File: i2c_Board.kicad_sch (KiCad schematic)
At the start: 18 parts, among them J1 Conn_01x10_Pin, J2 Logic Analyzer Connector Pins, U1 MCP9808_MSOP, U2 MCP7940N-xMS, Y1 Crystal

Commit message: Updated footprints
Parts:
- removed J1: Conn_01x10_Pin, Connector_PinHeader_1.00mm:PinHeader_1x10_P1.00mm_Vertical, symbol Connector:Conn_01x10_Pin
- added H1, H2, H3, H4: MountingHole_Pad, MountingHole:MountingHole_2.2mm_M2_DIN965_Pad, symbol Mechanical:MountingHole_Pad
- added J1: Conn_01x09_Pin, Connector_PinHeader_2.54mm:PinHeader_1x09_P2.54mm_Vertical, symbol Connector:Conn_01x09_Pin
- BT1: footprint Battery:BatteryHolder_Keystone_3002_1x2032 -> BAT-HLD-002-SMT:BAT_BAT-HLD-002-SMT; symbol Device:Battery_Cell -> BAT-HLD-002-SMT:BAT-HLD-002-SMT; Availability (none) -> In Stock; Check_prices (none) -> https://www.snapeda.com/parts/BAT-HLD-002-SMT/TE+Connectivi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; Description_1 (none) -> Battery Holder Coin 20 SMT Nickel; MF (none) -> TE Connectivity; MP (none) -> BAT-HLD-002-SMT; Package (none) -> None; Price (none) -> None; Purchase-URL (none) -> https://www.snapeda.com/api/url_track_click_mouser/?unipart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; SnapEDA_Link (none) -> https://www.snapeda.com/parts/BAT-HLD-002-SMT/TE+Connectivi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
- J2: footprint Connector_PinHeader_1.00mm:PinHeader_1x02_P1.00mm_Vertical -> Connector_PinHeader_2.54mm:PinHeader_1x02_P2.54mm_Vertical
- U1: value MCP9808_MSOP -> MCP9808
- U2: value MCP7940N-xMS -> MCP7940N
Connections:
- net +5V: now also J1.1 (Pin_1)
- net Address_0: now also J1.2 (Pin_2)
- net Address_1: now also J1.3 (Pin_3)
- net Address_2: now also J1.4 (Pin_4)
- net GND: now also BT1.P1, BT1.P2, H1.1, H2.1, H3.1, H4.1, J1.8 (Pin_8), J1.9 (Pin_9); no longer BT1.2 (-)
- net MCU_SCL: now also J1.6 (Pin_6)
- net MCU_SDA: now also J1.7 (Pin_7)
- net MFP: now also J1.5 (Pin_5)
- net at U2.3 (VBAT): now also BT1.N; no longer BT1.1 (+)

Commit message: Modified footprint & Rearranged routing
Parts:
- R5, R7: footprint Diode_SMD:D_0805_2012Metric_Pad1.15x1.40mm_HandSolder -> Resistor_SMD:R_0805_2012Metric_Pad1.20x1.40mm_HandSolder
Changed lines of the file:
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@@
 	(title_block
 		(title "I2C Testing Board")
-		(comment 1 "Add Connector Pin")
-		(comment 2 "Add Custom Name to PCB")
 	)
 	(junction
@@
 			)
 		)
-		(property "Footprint" "Diode_SMD:D_0805_2012Metric_Pad1.15x1.40mm_HandSolder"
+		(property "Footprint" "Resistor_SMD:R_0805_2012Metric_Pad1.20x1.40mm_HandSolder"
 			(at 97.79 50.038 90)
 			(effects
@@
 			)
 		)
-		(property "Footprint" "Diode_SMD:D_0805_2012Metric_Pad1.15x1.40mm_HandSolder"
+		(property "Footprint" "Resistor_SMD:R_0805_2012Metric_Pad1.20x1.40mm_HandSolder"
 			(at 63.5 80.518 90)
 			(effects

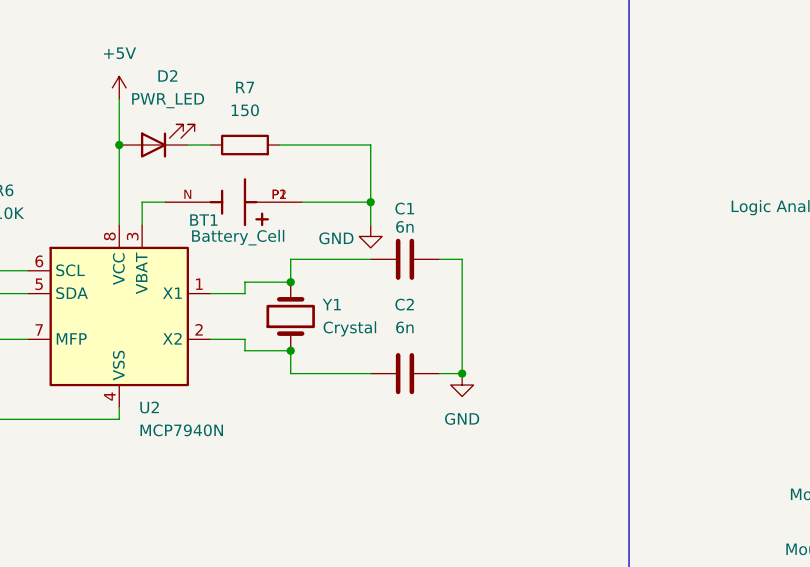
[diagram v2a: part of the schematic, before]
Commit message: Changed Capacitor value from 6nF to 6pF
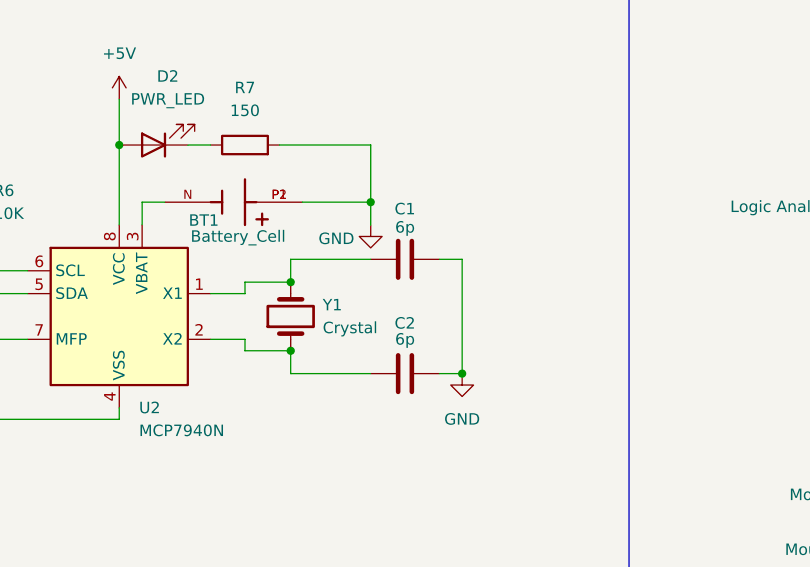
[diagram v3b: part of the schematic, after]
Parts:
- C1, C2: value 6n -> 6p
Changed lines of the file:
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@@
 		(on_board yes)
 		(dnp no)
-		(fields_autoplaced yes)
 		(property "Reference" "C2"
-			(at 115.57 66.04 90)
-			(effects
-				(font
-					(size 1.27 1.27)
-				)
-			)
-		)
-		(property "Value" "6n"
-			(at 115.57 68.58 90)
+			(at 115.57 68.072 90)
+			(effects
+				(font
+					(size 1.27 1.27)
+				)
+			)
+		)
+		(property "Value" "6p"
+			(at 115.57 69.85 90)
 			(effects
 				(font
@@
 			)
 		)
-		(property "Value" "6n"
+		(property "Value" "6p"
 			(at 115.57 57.404 90)
 			(effects

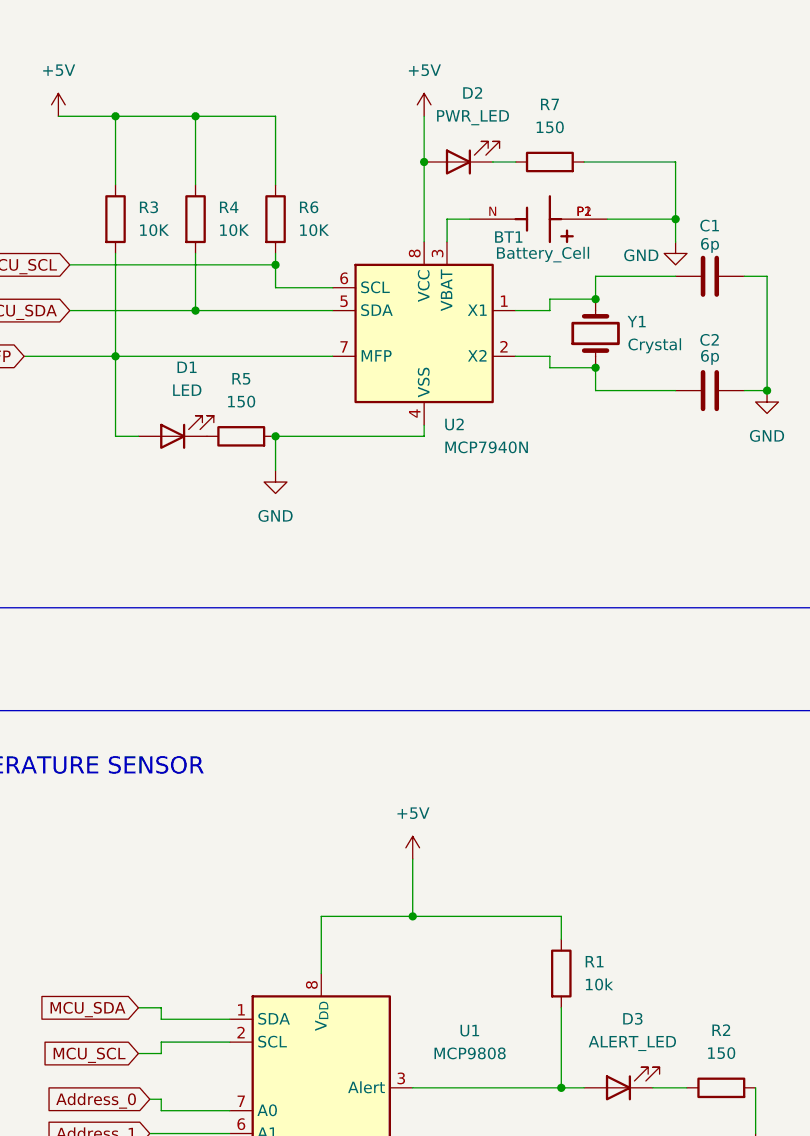
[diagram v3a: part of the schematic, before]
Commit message: Added Decoupling Capacitors
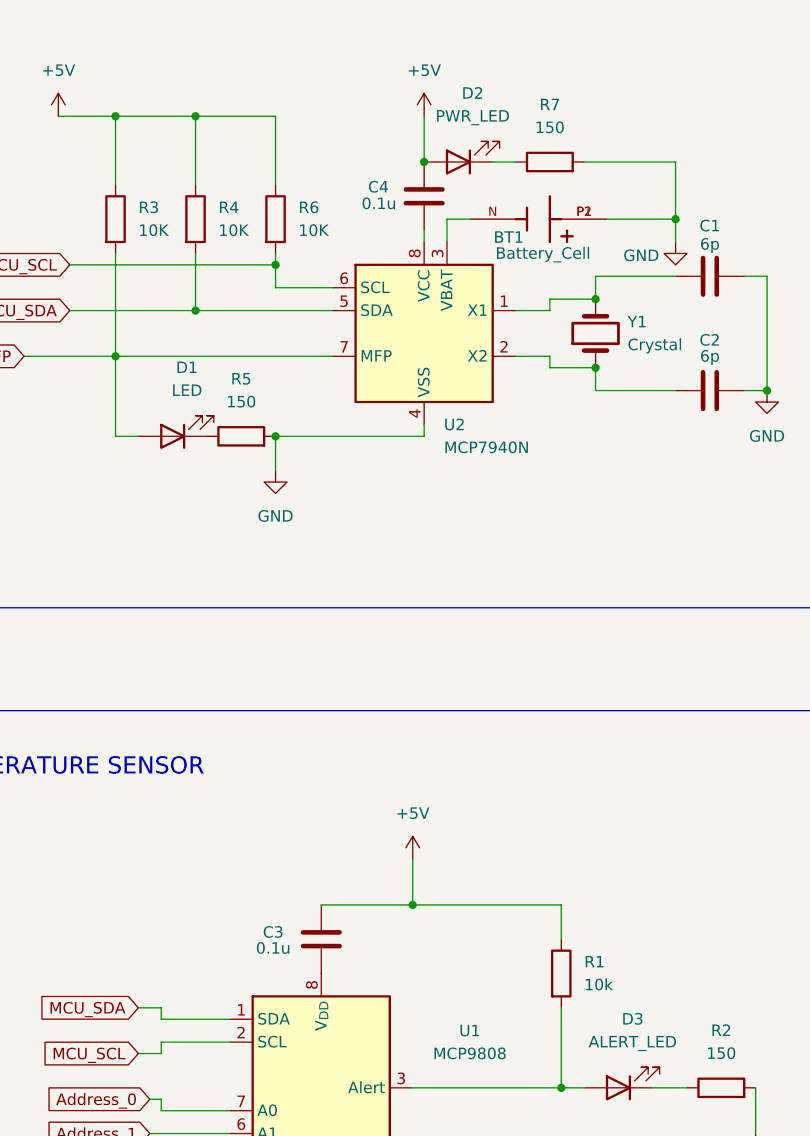
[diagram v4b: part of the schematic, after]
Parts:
- added C3, C4: 0.1u, Capacitor_SMD:C_0805_2012Metric_Pad1.18x1.45mm_HandSolder, symbol Device:C
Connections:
- net +5V: now also C3.1, C4.1; no longer U1.8 (V_{DD}), U2.8 (VCC)
- new net: C4.2, U2.8 (VCC)
- new net: C3.2, U1.8 (V_{DD})
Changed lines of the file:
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@@
 	)
 	(junction
-		(at 82.55 132.08)
-		(diameter 0)
-		(color 0 0 0 0)
-	)
-	(junction
 		(at 186.69 86.36)
 		(diameter 0)
@@
 	)
 	(junction
+		(at 82.55 130.81)
+		(diameter 0)
+		(color 0 0 0 0)
+	)
+	(junction
 		(at 83.82 48.26)
 		(diameter 0)
@@
 	(wire
 		(pts
-			(xy 72.39 138.43) (xy 72.39 132.08)
-		)
-		(stroke
-			(width 0)
-			(type default)
-		)
-	)
-	(wire
-		(pts
 			(xy 187.96 64.77) (xy 175.26 64.77)
 		)
@@
 	(wire
 		(pts
-			(xy 99.06 132.08) (xy 99.06 134.62)
+			(xy 99.06 130.81) (xy 99.06 134.62)
 		)
 		(stroke
@@
 	(wire
 		(pts
+			(xy 83.82 55.88) (xy 83.82 57.15)
+		)
+		(stroke
+			(width 0)
+			(type default)
+		)
+	)
+	(wire
+		(pts
 			(xy 175.26 60.96) (xy 187.96 60.96)
 		)
@@
 	(wire
 		(pts
-			(xy 72.39 132.08) (xy 82.55 132.08)
+			(xy 72.39 130.81) (xy 82.55 130.81)
 		)
 		(stroke
@@
 	(wire
 		(pts
-			(xy 82.55 132.08) (xy 99.06 132.08)
+			(xy 82.55 130.81) (xy 99.06 130.81)
 		)
 		(stroke
@@
 	(wire
 		(pts
-			(xy 82.55 125.73) (xy 82.55 132.08)
-		)
-		(stroke
-			(width 0)
-			(type default)
-		)
-	)
-	(wire
-		(pts
-			(xy 83.82 48.26) (xy 83.82 57.15)
+			(xy 82.55 125.73) (xy 82.55 130.81)
 		)
 		(stroke
@@
 	)
 	(symbol
+		(lib_id "Device:C")
+		(at 72.39 134.62 0)
+		(unit 1)
+		(exclude_from_sim no)
+		(in_bom yes)
+		(on_board yes)
+		(dnp no)
+		(property "Reference" "C3"
+			(at 67.056 133.858 0)
+			(effects
+				(font
+					(size 1.27 1.27)
+				)
+			)
+		)
+		(property "Value" "0.1u"
+			(at 67.056 135.636 0)
+			(effects
+				(font
+					(size 1.27 1.27)
+				)
+			)
+		)
+		(property "Footprint" "Capacitor_SMD:C_0805_2012Metric_Pad1.18x1.45mm_HandSolder"
+			(at 73.3552 138.43 0)
+			(effects
+				(font
+					(size 1.27 1.27)
+				)
+				(hide yes)
+			)
+		)
+		(property "Datasheet" "~"
+			(at 72.39 134.62 0)
+			(effects
+				(font
+					(size 1.27 1.27)
+				)
+				(hide yes)
+			)
+		)
+		(property "Description" "Unpolarized capacitor"
+			(at 72.39 134.62 0)
+			(effects
+				(font
+					(size 1.27 1.27)
+				)
+				(hide yes)
+			)
+		)
+		(pin "1"
+		)
+		(pin "2"
+		)
+		(instances
+			(project "i2c_Board"
+				(path "/853e014d-ba1a-4791-8d4a-2caab7ca8c76"
+					(reference "C3")
+					(unit 1)
+				)
+			)
+		)
+	)
+	(symbol
 		(lib_id "Device:LED")
 		(at 87.63 48.26 180)
@@
 					(unit 1)
 				)
+			)
+		)
+	)
+	(symbol
+		(lib_id "Device:C")
+		(at 83.82 52.07 0)
+		(unit 1)
+		(exclude_from_sim no)
+		(in_bom yes)
+		(on_board yes)
+		(dnp no)
+		(property "Reference" "C4"
+			(at 78.74 51.054 0)
+			(effects
+				(font
+					(size 1.27 1.27)
+				)
+			)
+		)
+		(property "Value" "0.1u"
+			(at 78.8035 52.8955 0)
+			(effects
+				(font
+					(size 1.27 1.27)
+				)
+			)
+		)
+		(property "Footprint" "Capacitor_SMD:C_0805_2012Metric_Pad1.18x1.45mm_HandSolder"
+			(at 84.7852 55.88 0)
+			(effects
+				(font
+					(size 1.27 1.27)
+				)
+				(hide yes)
+			)
+		)
+		(property "Datasheet" "~"
+			(at 83.82 52.07 0)
+			(effects
+				(font
+					(size 1.27 1.27)
+				)
+				(hide yes)
+			)
+		)
+		(property "Description" "Unpolarized capacitor"
+			(at 83.82 52.07 0)
+			(effects
+				(font
+					(size 1.27 1.27)
+				)
+				(hide yes)
+			)
+		)
+		(pin "1"
+		)
+		(pin "2"
+		)
+		(instances
+			(project "i2c_Board"
+				(path "/853e014d-ba1a-4791-8d4a-2caab7ca8c76"
+					(reference "C4")
+					(unit 1)
+				)

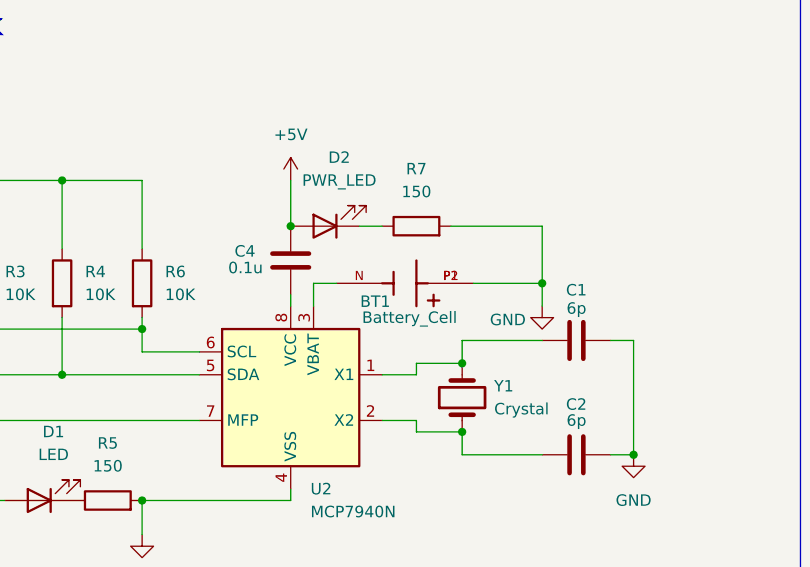
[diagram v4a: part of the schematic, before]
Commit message: Flipped incorrect battery polarity
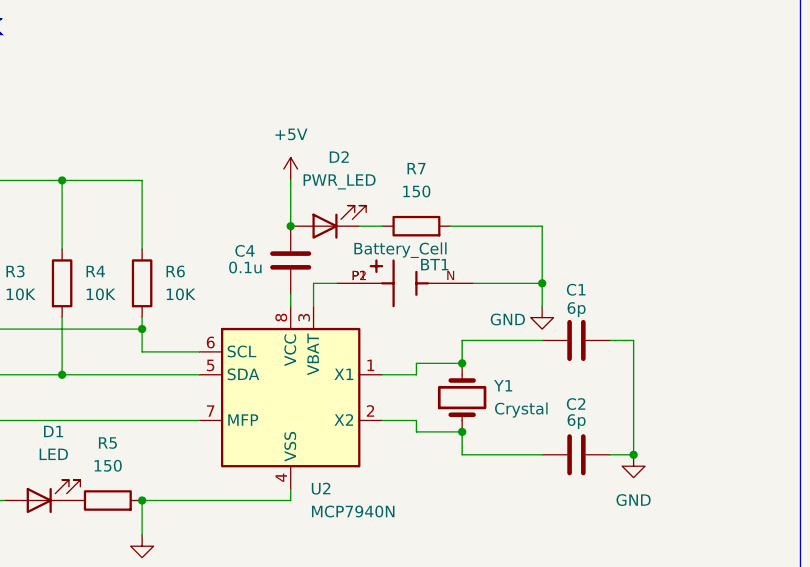
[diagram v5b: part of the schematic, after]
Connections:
- net GND: now also BT1.N; no longer BT1.P1, BT1.P2
- net at U2.3 (VBAT): now also BT1.P1, BT1.P2; no longer BT1.N
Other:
- moved on the sheet: BT1
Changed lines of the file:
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@@
 	(symbol
 		(lib_id "BAT-HLD-002-SMT:BAT-HLD-002-SMT")
-		(at 96.52 54.61 180)
+		(at 96.52 54.61 0)
 		(unit 1)
 		(exclude_from_sim no)
@@
 		(dnp no)
 		(property "Reference" "BT1"
-			(at 93.218 56.642 0)
+			(at 99.822 52.578 0)
 			(effects
 				(font
@@
 		)
 		(property "Value" "Battery_Cell"
-			(at 97.028 58.42 0)
+			(at 96.012 50.8 0)
 			(effects
 				(font
